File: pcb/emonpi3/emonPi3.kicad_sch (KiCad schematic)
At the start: 112 parts, among them CN1 Screw_Terminal_01x06, CN3 CONN_03SCREW, J10 Conn_ARM_JTAG_SWD_10, J12 Conn_02x20_Odd_Even, J13 Conn_02x05_Odd_Even, J7 CONN_04PTH, J8 CONN_04PTH, J9 USB_C_Receptacle_USB2.0, SW1 SW_Push, SW3 SW_Push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

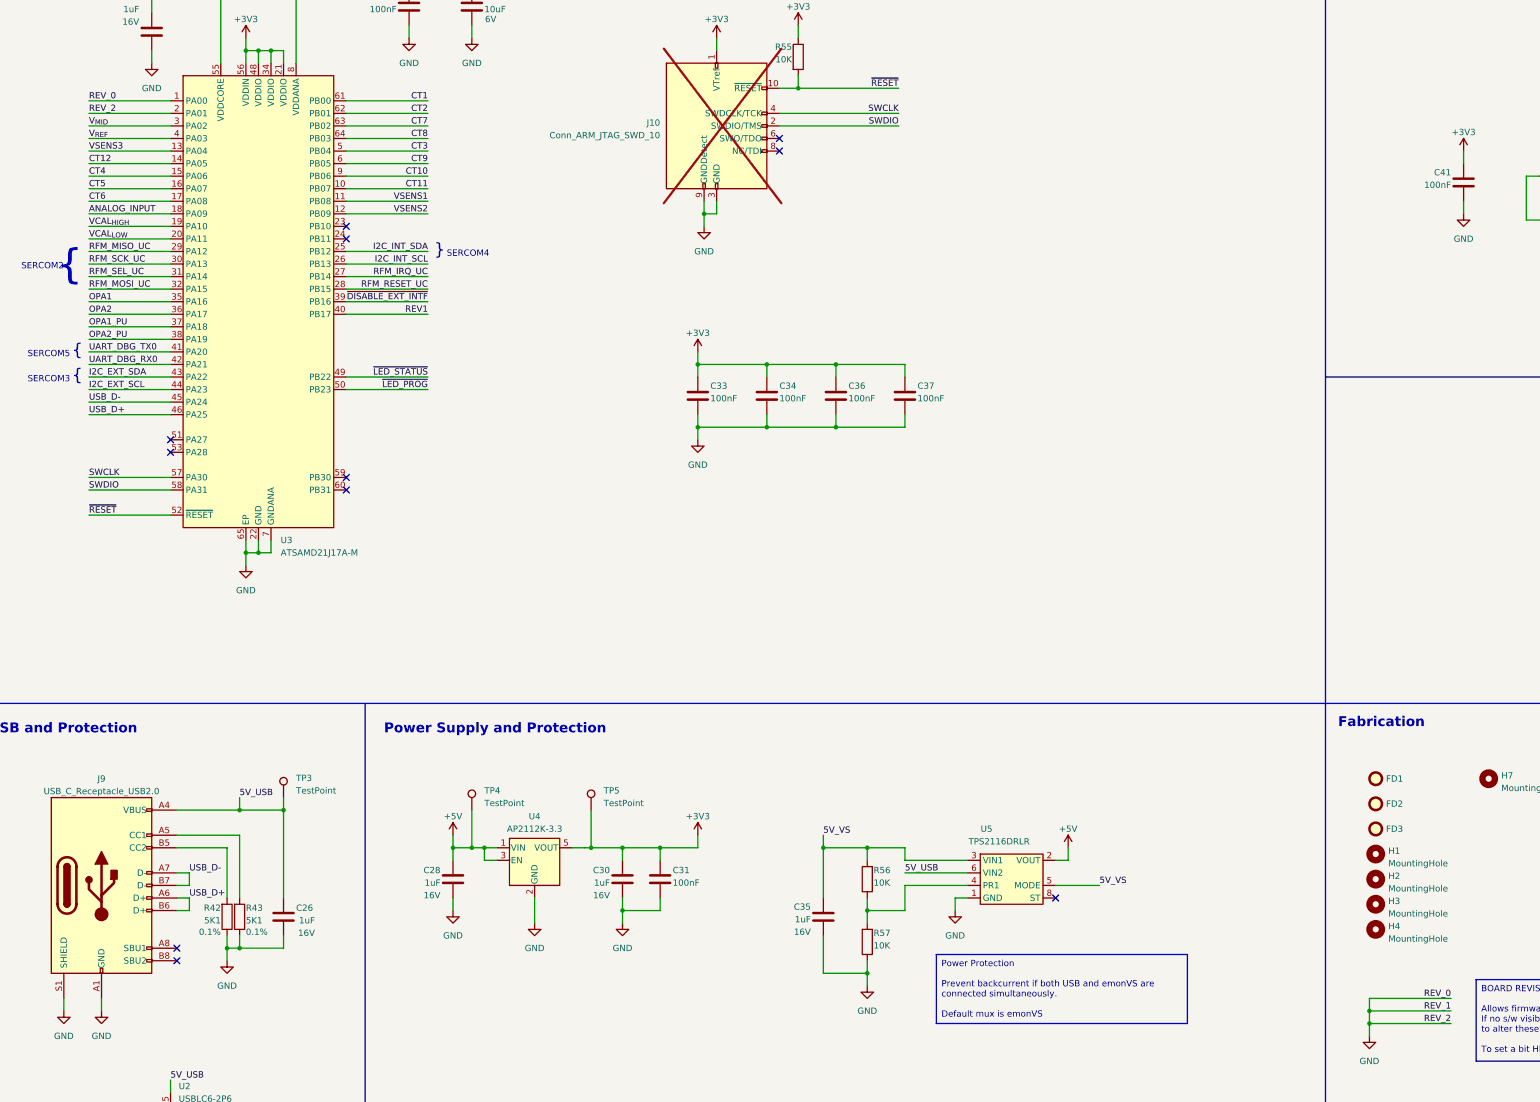
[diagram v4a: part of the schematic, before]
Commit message: * [v1.0] First v0.2 -> v1.0 revisions
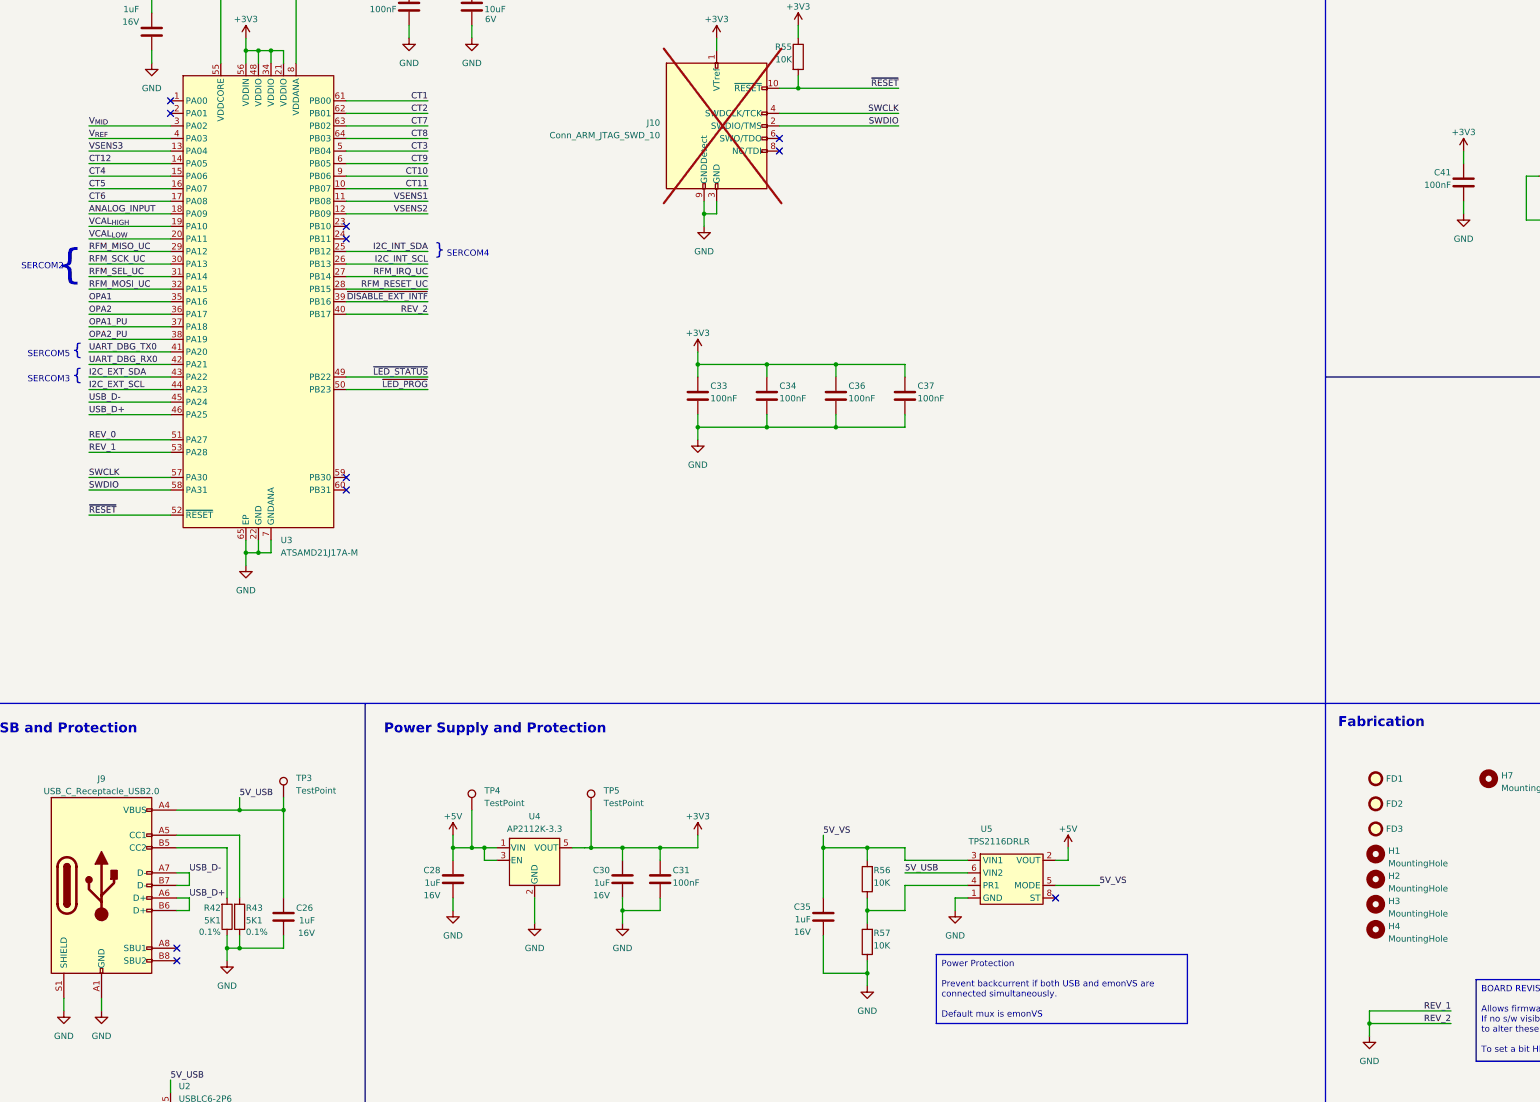
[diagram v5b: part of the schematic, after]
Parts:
- CN1: MPN (none) -> 5441388; Manufacturer (none) -> Pheonix Contact; Mouser (none) -> 651-5441388
- CN3: MPN (none) -> 5441359; Manufacturer (none) -> Pheonix Contact; Mouser (none) -> 651-5441359
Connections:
- net REV1 is gone; now on net GND: U3.40 (PB17)
- net GND: now also U3.53 (PA28); no longer U3.1 (PA00), U3.2 (PA01)
- net REV_0: now reaches U3.51 (PA27)
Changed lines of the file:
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@@
   (junction (at 165.1 245.11) (diameter 0) (color 0 0 0 0)
   )
-  (junction (at 482.6 356.87) (diameter 0) (color 0 0 0 0)
-  )
   (junction (at 381 336.55) (diameter 0) (color 0 0 0 0)
   )
@@
   (no_connect (at 406.4 30.48))
   (no_connect (at 419.1 76.2))
-  (no_connect (at 240.03 243.84))
   (no_connect (at 275.59 248.92))
   (no_connect (at 537.21 71.12))
@@
   (no_connect (at 419.1 68.58))
   (no_connect (at 419.1 60.96))
-  (no_connect (at 240.03 241.3))
   (no_connect (at 406.4 50.8))
   (no_connect (at 537.21 76.2))
+  (no_connect (at 240.03 175.26))
   (no_connect (at 241.3 344.17))
   (no_connect (at 275.59 200.66))
@@
   (no_connect (at 406.4 71.12))
   (no_connect (at 363.22 180.34))
+  (no_connect (at 240.03 172.72))
   (no_connect (at 275.59 198.12))
   (no_connect (at 406.4 66.04))
@@
     (stroke (width 0.1524) (type solid))
   )
-  (wire (pts (xy 482.6 354.33) (xy 482.6 356.87))
-    (stroke (width 0) (type default))
-  )
   (wire (pts (xy 161.29 193.04) (xy 161.29 195.58))
     (stroke (width 0) (type default))
@@
     (stroke (width 0) (type default))
   )
+  (wire (pts (xy 223.52 243.84) (xy 240.03 243.84))
+    (stroke (width 0) (type default))
+  )
   (wire (pts (xy 254 321.31) (xy 254 334.01))
     (stroke (width 0) (type default))
@@
     (stroke (width 0) (type default))
   )
-  (wire (pts (xy 482.6 354.33) (xy 499.11 354.33))
-    (stroke (width 0) (type default))
-  )
   (wire (pts (xy 339.09 336.55) (xy 339.09 334.01))
     (stroke (width 0.1524) (type solid))
@@
     (stroke (width 0) (type default))
   )
-  (wire (pts (xy 223.52 175.26) (xy 240.03 175.26))
-    (stroke (width 0) (type default))
-  )
   (wire (pts (xy 176.53 60.96) (xy 184.15 60.96))
     (stroke (width 0.1524) (type solid))
@@
     (stroke (width 0.1524) (type solid))
   )
-  (wire (pts (xy 223.52 172.72) (xy 240.03 172.72))
-    (stroke (width 0) (type default))
-  )
   (wire (pts (xy 283.21 33.02) (xy 283.21 29.21))
     (stroke (width 0.1524) (type solid))
@@
     (stroke (width 0) (type default))
   )
+  (wire (pts (xy 223.52 241.3) (xy 240.03 241.3))
+    (stroke (width 0) (type default))
+  )
   (wire (pts (xy 347.98 193.04) (xy 347.98 195.58))
     (stroke (width 0) (type default))
@@
     (effects (font (size 1.2446 1.2446)) (justify right bottom))
   )
-  (label "REV_0" (at 223.52 172.72 0) (fields_autoplaced)
+  (label "REV_0" (at 223.52 241.3 0) (fields_autoplaced)
     (effects (font (size 1.27 1.27)) (justify left bottom))
   )
@@
     (effects (font (size 1.27 1.27)) (justify right bottom))
   )
-  (label "REV1" (at 292.1 215.9 180) (fields_autoplaced)
-    (effects (font (size 1.27 1.27)) (justify right bottom))
+  (label "REV_1" (at 223.52 243.84 0) (fields_autoplaced)
+    (effects (font (size 1.27 1.27)) (justify left bottom))
   )
   (label "RFM_SEL" (at 487.68 74.93 0) (fields_autoplaced)
@@
     (effects (font (size 1.27 1.27)) (justify left bottom))
   )
-  (label "REV_2" (at 223.52 175.26 0) (fields_autoplaced)
-    (effects (font (size 1.27 1.27)) (justify left bottom))
+  (label "REV_2" (at 292.1 215.9 180) (fields_autoplaced)
+    (effects (font (size 1.27 1.27)) (justify right bottom))
   )
   (label "CT7" (at 292.1 177.8 180) (fields_autoplaced)
@@
     (effects (font (size 1.27 1.27)) (justify right bottom))
   )
-  (label "REV_0" (at 499.11 354.33 180) (fields_autoplaced)
-    (effects (font (size 1.27 1.27)) (justify right bottom))
-  )
   (label "RFM_SEL" (at 440.69 48.26 180) (fields_autoplaced)
     (effects (font (size 1.2446 1.2446)) (justify right bottom))
@@
       (effects (font (size 1.27 1.27)) hide)
     )
+    (property "Manufacturer" "Pheonix Contact" (at 191.77 171.45 0)
+      (effects (font (size 1.27 1.27)) hide)
+    )
+    (property "MPN" "5441359" (at 191.77 171.45 0)
+      (effects (font (size 1.27 1.27)) hide)
+    )
+    (property "Mouser" "651-5441359" (at 191.77 171.45 0)
+      (effects (font (size 1.27 1.27)) hide)
+    )
     (pin "1")
     (pin "2")
@@
       (effects (font (size 1.27 1.27)) hide)
     )
+    (property "Manufacturer" "Pheonix Contact" (at 191.77 149.86 0)
+      (effects (font (size 1.27 1.27)) hide)
+    )
+    (property "MPN" "5441388" (at 191.77 149.86 0)
+      (effects (font (size 1.27 1.27)) hide)
+    )
+    (property "Mouser" "651-5441388" (at 191.77 149.86 0)
+      (effects (font (size 1.27 1.27)) hide)
+    )

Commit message: * Correct footprint for bicolour LED
  - KiCAD library footprint is incorrect.
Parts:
- LED5: footprint LED_SMD:LED_LiteOn_LTST-S326 -> ltst-s326:LTST-S326
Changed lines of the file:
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@@
       (effects (font (size 1.27 1.27)) (justify left))
     )
-    (property "Footprint" "LED_SMD:LED_LiteOn_LTST-S326" (at 289.56 97.79 0)
+    (property "Footprint" "ltst-s326:LTST-S326" (at 289.56 97.79 0)
       (effects (font (size 1.27 1.27)) hide)
     )

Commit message: * Add additional user measurements and documentation
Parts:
- added C9: 10uF, Capacitor_SMD:C_0603_1608Metric, symbol Device:C
- added TP10, TP11, TP7, TP8, TP9: TestPoint, TestPoint:TestPoint_Pad_D1.0mm, symbol Connector:TestPoint
- J8, SW1: now not fitted
- U1: value MCP1501-10xCH -> MCP1501T-10E/CHY
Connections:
- net +5V: now also C9.1
- net GND: now also C9.2, TP10.1, TP11.1
- net VCAL_{HIGH}: now also TP8.1
- net VCAL_{LOW}: now also TP9.1
- net VSENS1: now also TP7.1
